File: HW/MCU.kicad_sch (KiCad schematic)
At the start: 6 parts, among them U5 STM32C011F4P6

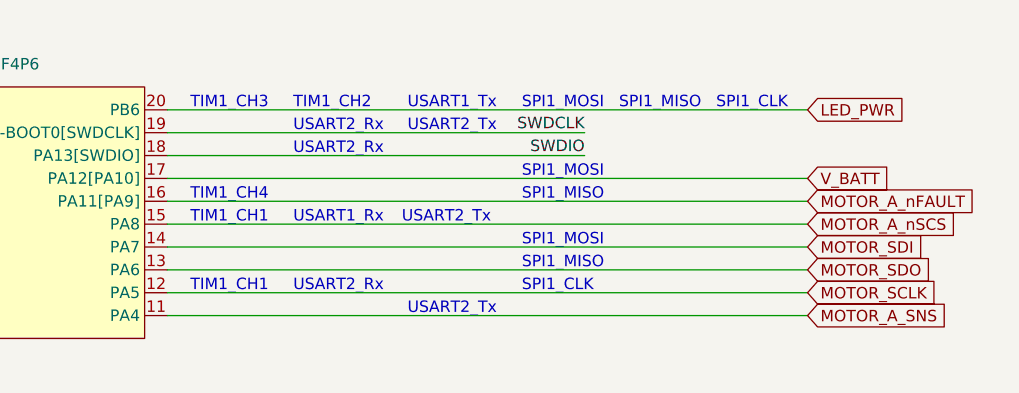
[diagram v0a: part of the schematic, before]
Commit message: WIP - Layout XT30/PCB Finger Positions
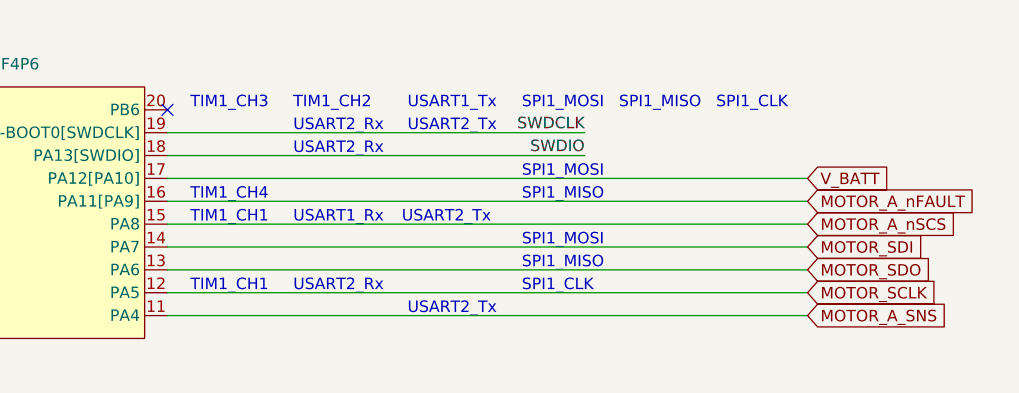
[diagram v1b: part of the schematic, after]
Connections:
- net LED_PWR: no longer names the net of U5.20 (PB6)
- no-connect marks 0 -> 1
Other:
- title: WEKA ESC - 20A -> KAKAPO ESC - 20A
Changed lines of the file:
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@@
   (paper "A4")
   (title_block
-    (title "WEKA ESC - 20A")
-    (date "2024-01-06")
-    (rev "v2.0")
+    (title "KAKAPO ESC - 20A")
+    (date "2024-03-10")
+    (rev "v1.0")
     (company "CB-TECHNOLOGY")
   )
   (junction (at 53.34 162.56) (diameter 0) (color 0 0 0 0)
   )
+  (no_connect (at 165.1 83.82))
   (wire (pts (xy 52.07 172.72) (xy 63.5 172.72))
     (stroke (width 0) (type default))
@@
   )
   (wire (pts (xy 71.755 99.06) (xy 121.92 99.06))
-    (stroke (width 0) (type default))
-  )
-  (wire (pts (xy 165.1 83.82) (xy 236.22 83.82))
     (stroke (width 0) (type default))
   )
@@
     )
   )
-  (global_label "LED_PWR" (shape input) (at 236.22 83.82 0) (fields_autoplaced)
-    (effects (font (size 1.27 1.27)) (justify left))
-    (property "Intersheetrefs" "${INTERSHEET_REFS}" (at 247.6113 83.82 0)
-      (effects (font (size 1.27 1.27)) (justify left))
-    )
-  )
   (global_label "MOTOR_B_nSCS" (shape input) (at 71.755 86.36 180) (fields_autoplaced)
     (effects (font (size 1.27 1.27)) (justify right))
@@
     (pin "1")
     (instances
-      (project "WEKA_ESC-20A"
+      (project "KAKAPO_ESC-20A"
         (path "/e63e39d7-6ac0-4ffd-8aa3-1841a4541b55/21a04b71-f06d-40d5-93cd-e1812c0e9089"
           (reference "TP4") (unit 1)
@@
     (pin "2")
     (instances
-      (project "WEKA_ESC-20A"
+      (project "KAKAPO_ESC-20A"
         (path "/e63e39d7-6ac0-4ffd-8aa3-1841a4541b55/21a04b71-f06d-40d5-93cd-e1812c0e9089"
           (reference "C14") (unit 1)
@@
     (pin "1")
     (instances
-      (project "WEKA_ESC-20A"
+      (project "KAKAPO_ESC-20A"
         (path "/e63e39d7-6ac0-4ffd-8aa3-1841a4541b55/21a04b71-f06d-40d5-93cd-e1812c0e9089"
           (reference "#PWR01") (unit 1)
@@
     (pin "1")
     (instances
-      (project "WEKA_ESC-20A"
+      (project "KAKAPO_ESC-20A"
         (path "/e63e39d7-6ac0-4ffd-8aa3-1841a4541b55/21a04b71-f06d-40d5-93cd-e1812c0e9089"
           (reference "TP3") (unit 1)
@@
     (pin "1")
     (instances
-      (project "WEKA_ESC-20A"
+      (project "KAKAPO_ESC-20A"
         (path "/e63e39d7-6ac0-4ffd-8aa3-1841a4541b55/21a04b71-f06d-40d5-93cd-e1812c0e9089"
           (reference "TP1") (unit 1)
@@
     (pin "1")
     (instances
-      (project "WEKA_ESC-20A"
+      (project "KAKAPO_ESC-20A"
         (path "/e63e39d7-6ac0-4ffd-8aa3-1841a4541b55/21a04b71-f06d-40d5-93cd-e1812c0e9089"
           (reference "TP2") (unit 1)
@@
     (pin "9")
     (instances
-      (project "WEKA_ESC-20A"
+      (project "KAKAPO_ESC-20A"
         (path "/e63e39d7-6ac0-4ffd-8aa3-1841a4541b55/21a04b71-f06d-40d5-93cd-e1812c0e9089"
           (reference "U5") (unit 1)
@@
     (pin "1")
     (instances
-      (project "WEKA_ESC-20A"
+      (project "KAKAPO_ESC-20A"
         (path "/e63e39d7-6ac0-4ffd-8aa3-1841a4541b55/21a04b71-f06d-40d5-93cd-e1812c0e9089"
           (reference "#PWR031") (unit 1)
@@
     (pin "1")
     (instances
-      (project "WEKA_ESC-20A"
+      (project "KAKAPO_ESC-20A"
         (path "/e63e39d7-6ac0-4ffd-8aa3-1841a4541b55/21a04b71-f06d-40d5-93cd-e1812c0e9089"
           (reference "#PWR07") (unit 1)
@@
     (pin "1")
     (instances
-      (project "WEKA_ESC-20A"
+      (project "KAKAPO_ESC-20A"
         (path "/e63e39d7-6ac0-4ffd-8aa3-1841a4541b55/21a04b71-f06d-40d5-93cd-e1812c0e9089"
           (reference "#PWR09") (unit 1)

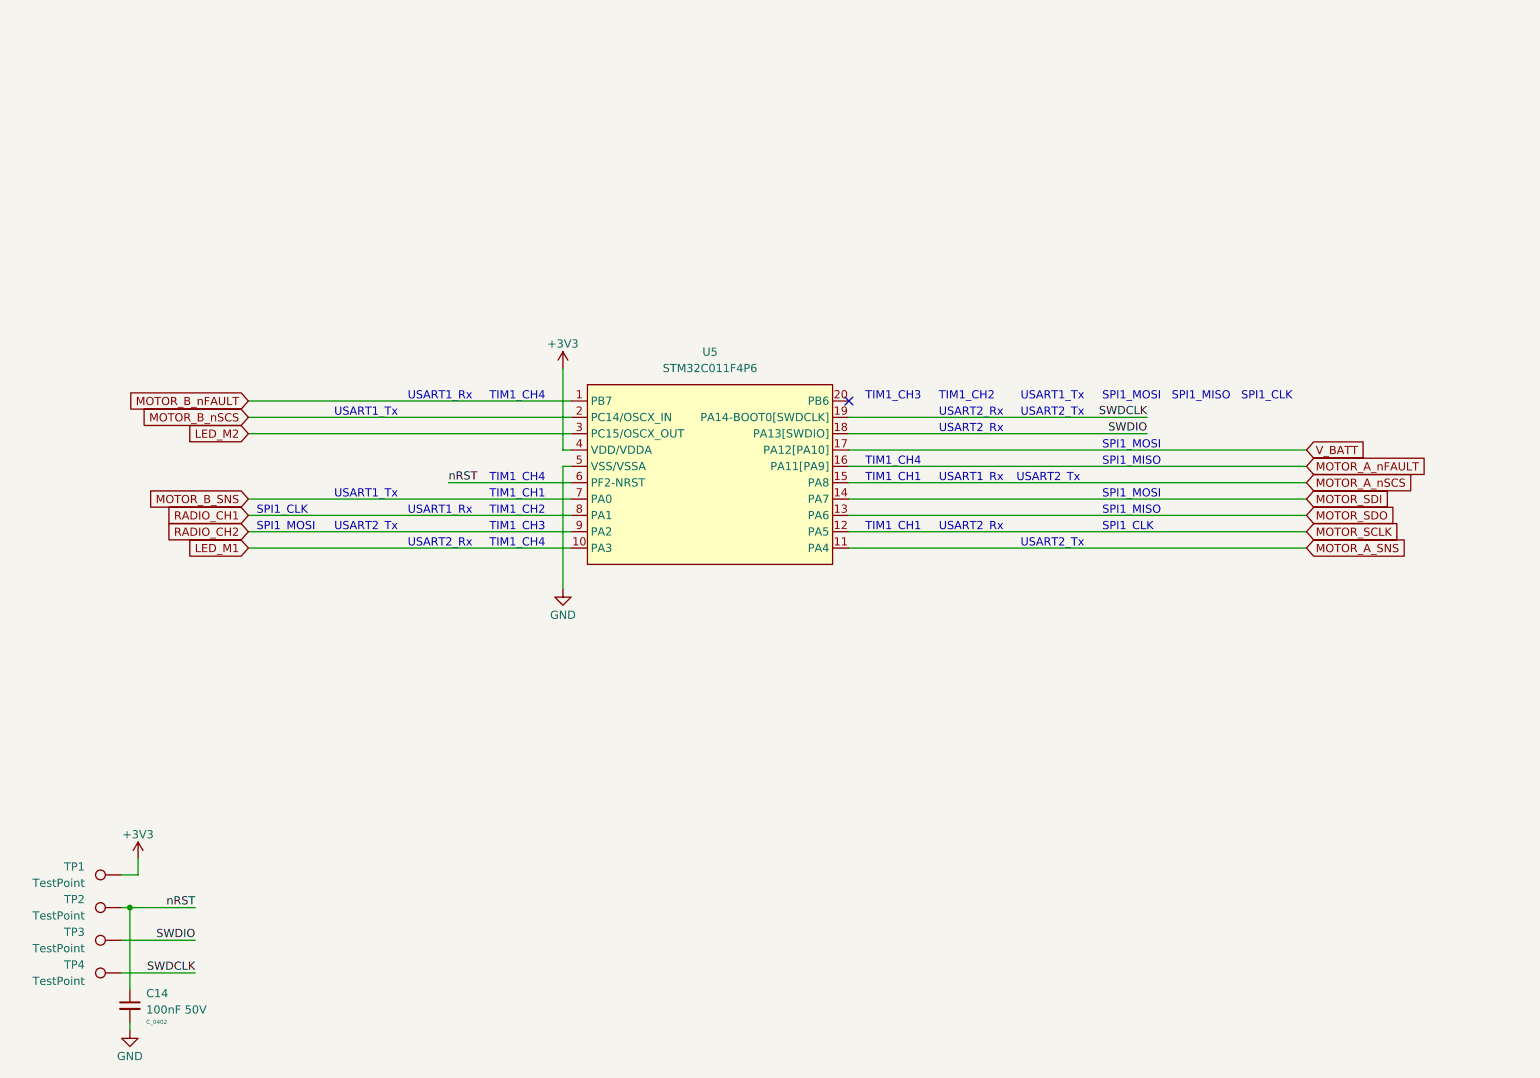
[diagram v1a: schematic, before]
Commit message: WIP - Layout Motor Drivers + Buck Circuit
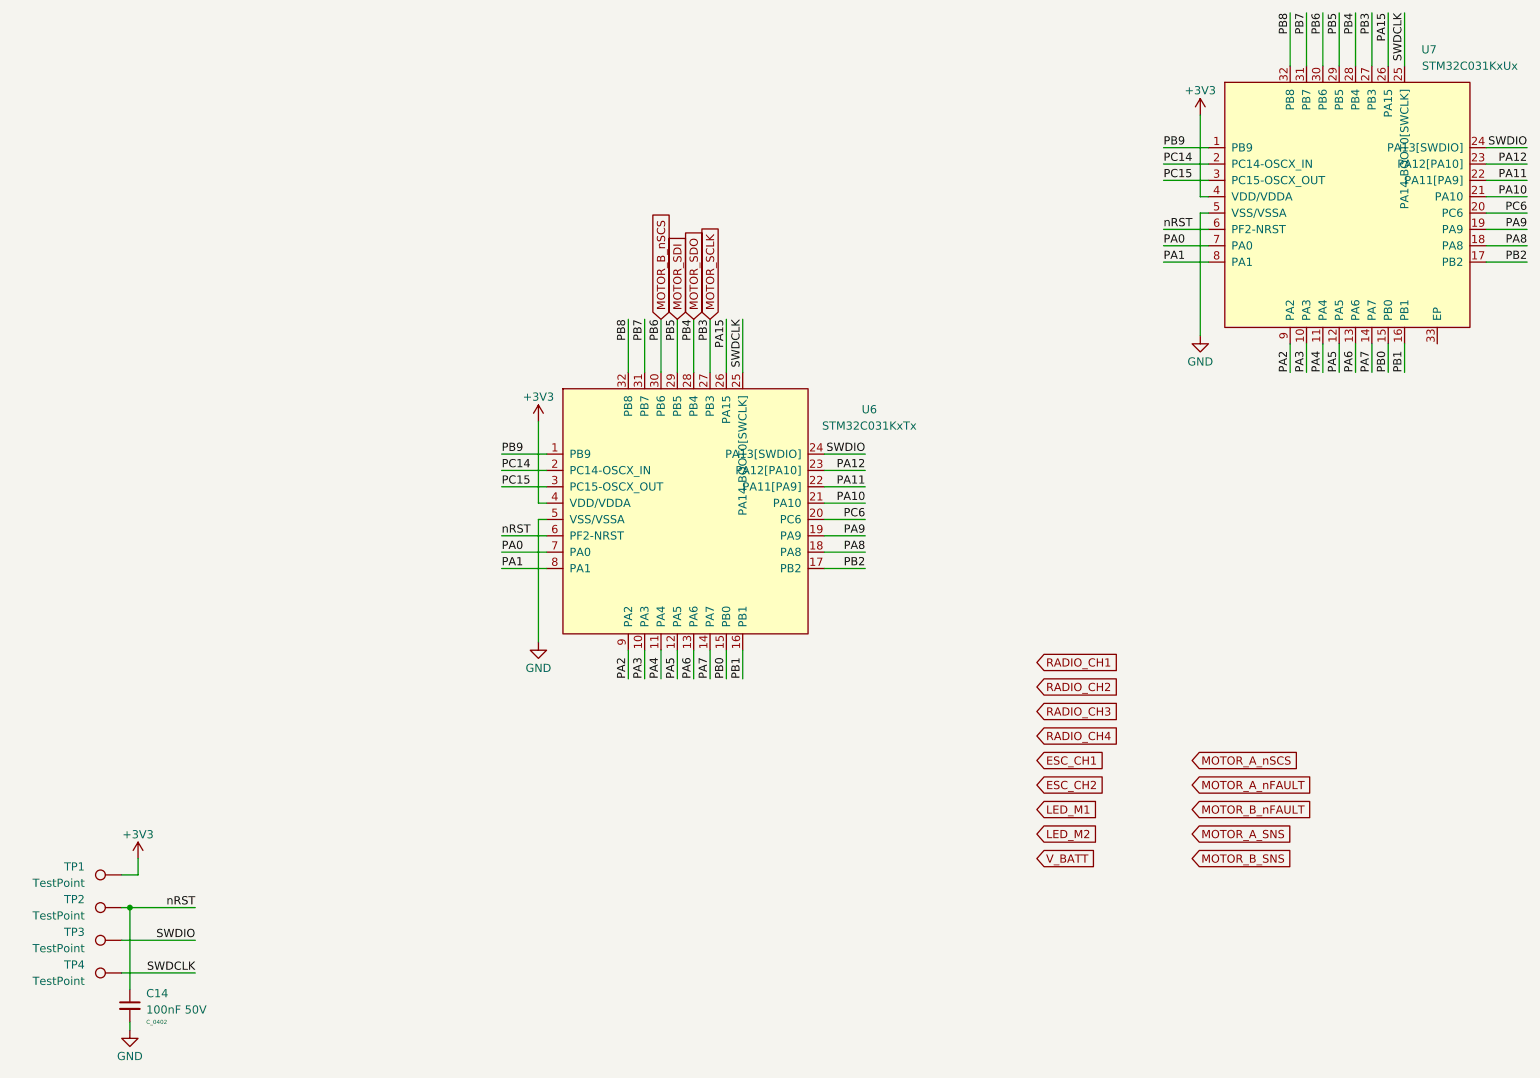
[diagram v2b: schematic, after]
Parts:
- removed U5: STM32C011F4P6, U_IC:TSSOP20_4.4mm, symbol U_MCU:STM32C031FxPx
- added U6: STM32C031KxTx, U_IC:LQFP32_08_7x7, symbol U_MCU:STM32C031KxTx
- added U7: STM32C031KxUx, U_IC:QFN32_05_5x5_EP, symbol U_MCU:STM32C031KxUx
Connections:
- net +3V3: now also U6.4 (VDD/VDDA), U7.4 (VDD/VDDA)
- net GND: now also U6.5 (VSS/VSSA), U7.5 (VSS/VSSA)
- net MOTOR_B_nSCS: now also U6.30 (PB6), U7.30 (PB6)
- net MOTOR_SCLK: now also U6.27 (PB3), U7.27 (PB3)
- net MOTOR_SDI: now also U6.29 (PB5), U7.29 (PB5)
- net MOTOR_SDO: now also U6.28 (PB4), U7.28 (PB4)
- net SWDCLK: now also U6.25 (PA14-BOOT0[SWCLK]), U7.25 (PA14-BOOT0[SWCLK])
- net SWDIO: now also U6.24 (PA13[SWDIO]), U7.24 (PA13[SWDIO])
- net nRST: now also U6.6 (PF2-NRST), U7.6 (PF2-NRST)
- new net PA0: U6.7 (PA0), U7.7 (PA0)
- new net PA1: U6.8 (PA1), U7.8 (PA1)
- new net PA10: U6.21 (PA10), U7.21 (PA10)
- new net PA11: U6.22 (PA11[PA9]), U7.22 (PA11[PA9])
- new net PA12: U6.23 (PA12[PA10]), U7.23 (PA12[PA10])
- new net PA15: U6.26 (PA15), U7.26 (PA15)
- new net PA2: U6.9 (PA2), U7.9 (PA2)
- new net PA3: U6.10 (PA3), U7.10 (PA3)
- new net PA4: U6.11 (PA4), U7.11 (PA4)
- new net PA5: U6.12 (PA5), U7.12 (PA5)
- new net PA6: U6.13 (PA6), U7.13 (PA6)
- new net PA7: U6.14 (PA7), U7.14 (PA7)
- new net PA8: U6.18 (PA8), U7.18 (PA8)
- new net PA9: U6.19 (PA9), U7.19 (PA9)
- new net PB0: U6.15 (PB0), U7.15 (PB0)
- new net PB1: U6.16 (PB1), U7.16 (PB1)
- new net PB2: U6.17 (PB2), U7.17 (PB2)
- new net PB7: U6.31 (PB7), U7.31 (PB7)
- new net PB8: U6.32 (PB8), U7.32 (PB8)
- new net PB9: U6.1 (PB9), U7.1 (PB9)
- new net PC14: U6.2 (PC14-OSCX_IN), U7.2 (PC14-OSCX_IN)
- new net PC15: U6.3 (PC15-OSCX_OUT), U7.3 (PC15-OSCX_OUT)
- new net PC6: U6.20 (PC6), U7.20 (PC6)
- no-connect marks 1 -> 0
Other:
- note removed: "SPI1_CLK"
- note removed: "SPI1_MISO"
- note removed: "SPI1_MOSI"
- note removed: "TIM1_CH1"
- note removed: "TIM1_CH2"
- note removed: "TIM1_CH3"
- note removed: "TIM1_CH4"
- note removed: "USART1_Rx"
- note removed: "USART1_Tx"
- note removed: "USART2_Rx"
- note removed: "USART2_Tx"

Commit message: WIP - Final Detail Design Before Design Review
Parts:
- U7: now not fitted
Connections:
- net PA10 is gone; now on net RADIO_CH3: U6.21 (PA10), U7.21 (PA10)
- net PA11 is gone; now on net RADIO_CH4: U6.22 (PA11[PA9]), U7.22 (PA11[PA9])
- net PA12 is gone; now on net V_BATT: U6.23 (PA12[PA10]), U7.23 (PA12[PA10])
- net PA15 is gone; now on net MOTOR_B_nFAULT: U6.26 (PA15), U7.26 (PA15)
- net PA9 is gone; now on net RADIO_CH1: U6.19 (PA9), U7.19 (PA9)
- net PB7 is gone; now on net LED_M2: U6.31 (PB7), U7.31 (PB7)
- net PB8 is gone; now on net MOTOR_A_nFAULT: U6.32 (PB8), U7.32 (PB8)
- net PB9 is gone; now on net MOTOR_A_nSCS: U6.1 (PB9), U7.1 (PB9)
- net PC14 is gone; now on net LED_M1: U6.2 (PC14-OSCX_IN), U7.2 (PC14-OSCX_IN)
- net PC6 is gone; now on net RADIO_CH2: U6.20 (PC6), U7.20 (PC6)
- net GND: now also U7.33 (EP)
